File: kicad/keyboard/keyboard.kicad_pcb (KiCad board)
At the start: 2 copper layers, 119 parts, among them SW1 MX_SWITCH, SW10 MX_SWITCH, SW11 MX_SWITCH, SW12 MX_SWITCH, SW13 MX_SWITCH, SW14 MX_SWITCH, SW15 MX_SWITCH, SW16 MX_SWITCH, SW17 MX_SWITCH, SW18 MX_SWITCH, SW19 MX_SWITCH, SW2 MX_SWITCH, SW20 MX_SWITCH, SW21 MX_SWITCH, SW22 MX_SWITCH, SW23 MX_SWITCH, SW24 MX_SWITCH, SW25 MX_SWITCH, SW26 MX_SWITCH, SW27 MX_SWITCH, SW28 MX_SWITCH, SW29 MX_SWITCH, SW3 MX_SWITCH, SW30 MX_SWITCH, SW31 MX_SWITCH, SW32 MX_SWITCH, SW33 MX_SWITCH, SW34 MX_SWITCH, SW35 MX_SWITCH, SW36 MX_SWITCH, SW37 MX_SWITCH, SW38 MX_SWITCH, SW39 MX_SWITCH, SW4 MX_SWITCH, SW40 MX_SWITCH, SW41 MX_SWITCH, SW42 MX_SWITCH, SW43 MX_SWITCH, SW44 MX_SWITCH, SW45 MX_SWITCH, SW46 MX_SWITCH, SW47 MX_SWITCH, SW48 MX_SWITCH, SW49 MX_SWITCH, SW5 MX_SWITCH, SW50 MX_SWITCH, SW51 MX_SWITCH, SW52 MX_SWITCH, SW53 MX_SWITCH, SW54 MX_SWITCH, SW55 MX_SWITCH, SW56 MX_SWITCH, SW57 MX_SWITCH, SW58 MX_SWITCH, SW59 MX_SWITCH, SW6 MX_SWITCH, SW7 MX_SWITCH, SW8 MX_SWITCH, SW9 MX_SWITCH

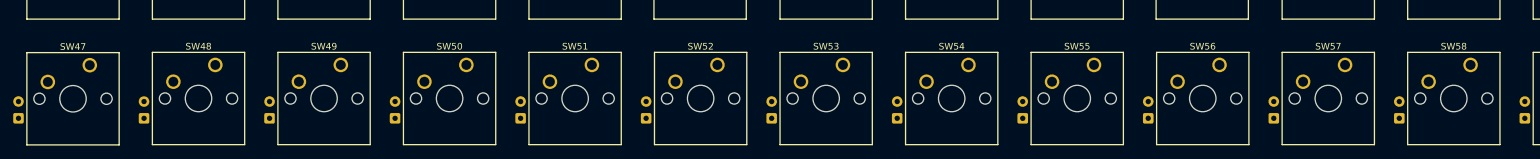
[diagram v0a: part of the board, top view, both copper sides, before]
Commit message: Fix incorrect switch positions
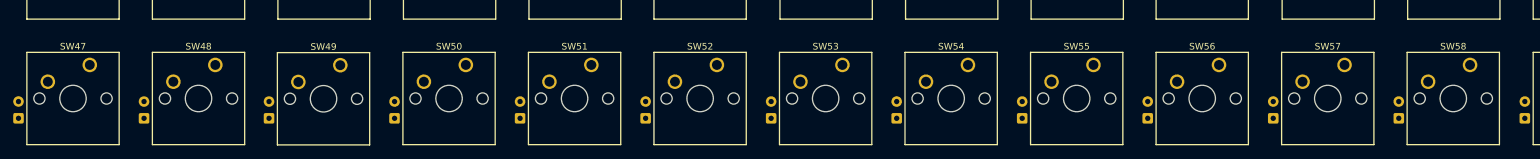
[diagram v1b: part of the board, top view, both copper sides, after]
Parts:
- SW1, SW10, SW11, SW12, SW13, SW14, SW15, SW16, SW17, SW18, SW19, SW2, SW20, SW21, SW22, SW23, SW24, SW25, SW26, SW27, SW28, SW29, SW3, SW30, SW31, SW32, SW33, SW34, SW35, SW36, SW37, SW38, SW39, SW4, SW40, SW41, SW42, SW43, SW44, SW5, SW59, SW6, SW7, SW8, SW9: value MX_SWITCH -> SW_MX
- SW45: renamed from SW56; value MX_SWITCH -> SW_MX
- SW46: renamed from SW58; value MX_SWITCH -> SW_MX
- SW47: renamed from SW45; value MX_SWITCH -> SW_MX
- SW48: renamed from SW46; value MX_SWITCH -> SW_MX
- SW49: renamed from SW47; value MX_SWITCH -> SW_MX
- SW50: renamed from SW48; value MX_SWITCH -> SW_MX
- SW51: renamed from SW49; value MX_SWITCH -> SW_MX
- SW52: renamed from SW50; value MX_SWITCH -> SW_MX
- SW53: renamed from SW51; value MX_SWITCH -> SW_MX
- SW54: renamed from SW52; value MX_SWITCH -> SW_MX
- SW55: renamed from SW53; value MX_SWITCH -> SW_MX
- SW56: renamed from SW54; value MX_SWITCH -> SW_MX
- SW57: renamed from SW55; value MX_SWITCH -> SW_MX
- SW58: renamed from SW57; value MX_SWITCH -> SW_MX
- moved SW48 209.9 mm to (61.0, 130.4)
- moved D47 209.9 mm to (31.2, 138.5)
- moved D48 209.9 mm to (50.2, 138.5)
- moved SW47 209.9 mm to (42.0, 130.4)
- moved D45 42.5 mm to (240.2, 119.5)
- moved SW45 42.5 mm to (251.0, 111.4)
- moved SW54 37.9 mm to (175.0, 130.4)
- moved SW55 37.9 mm to (194.0, 130.4)
- moved SW56 37.9 mm to (213.0, 130.4)
- moved SW57 37.9 mm to (232.0, 130.4)
- moved D49 37.9 mm to (69.2, 138.5)
- moved D50 37.9 mm to (88.2, 138.5)
- moved D51 37.9 mm to (107.2, 138.5)
- moved D52 37.9 mm to (126.2, 138.5)
- moved SW52 37.9 mm to (137.0, 130.4)
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- renumbered D56 to D45, D58 to D46, D45 to D47, D46 to D48, D47 to D49, D48 to D50, D49 to D51, D50 to D52, D51 to D53, D52 to D54, D53 to D55, D54 to D56, D55 to D57, D57 to D58

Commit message: Matrix traces
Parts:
- moved D1 16.7 mm to (47.8, 60.0)
- moved D12 16.7 mm to (47.8, 79.0)
- moved D23 16.7 mm to (47.8, 98.0)
- moved D47 16.7 mm to (47.8, 136.0)
- moved D34 16.7 mm to (47.8, 117.0)
- moved A1 0.38 mm to (248.9, 54.8)
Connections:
- A1 pad 10: COL7 -> COL6
- A1 pad 11: COL8 -> ROW3
- A1 pad 12: COL9 -> COL7
- A1 pad 14: COL10 -> COL8
- A1 pad 15: COL12 -> COL9
- A1 pad 16: COL11 -> COL10
- A1 pad 17: ROW0 -> unconnected-(A1-GPIO13-Pad17)
- A1 pad 19: ROW1 -> ROW2
- A1 pad 20: ROW2 -> unconnected-(A1-GPIO15-Pad20)
- A1 pad 21: ROW3 -> ROW0
- A1 pad 22: ROW4 -> ROW1
- A1 pad 24: unconnected-(A1-GPIO18-Pad24) -> COL11
- A1 pad 25: unconnected-(A1-GPIO19-Pad25) -> COL12
- A1 pad 4: COL2 -> ROW4
- A1 pad 5: COL3 -> COL2
- A1 pad 6: COL4 -> COL3
- A1 pad 7: COL5 -> COL4
- A1 pad 9: COL6 -> COL5
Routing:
- net ROW0: track 0.00 -> 212.7 mm
- net ROW1: track 0.00 -> 212.5 mm
- net ROW2: track 0.00 -> 174.7 mm
- net ROW4: track 0.00 -> 174.5 mm
- net ROW3: track 0.00 -> 174.5 mm
- net COL2: track 0.00 -> 76.1 mm
- net COL4: track 0.00 -> 76.0 mm
- net COL3: track 0.00 -> 76.0 mm
- net COL8: track 0.00 -> 76.0 mm
- net COL7: track 0.00 -> 76.0 mm
- net COL6: track 0.00 -> 76.0 mm
- net COL5: track 0.00 -> 76.0 mm
- net COL10: track 0.00 -> 76.0 mm
- net COL9: track 0.00 -> 76.0 mm
- net COL1: track 0.00 -> 76.0 mm
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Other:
- board outline added: 244 x 92 mm
